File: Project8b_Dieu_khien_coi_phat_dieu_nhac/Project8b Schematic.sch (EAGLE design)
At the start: 16 parts, among them U1 ARDUINOR3-BPLACE

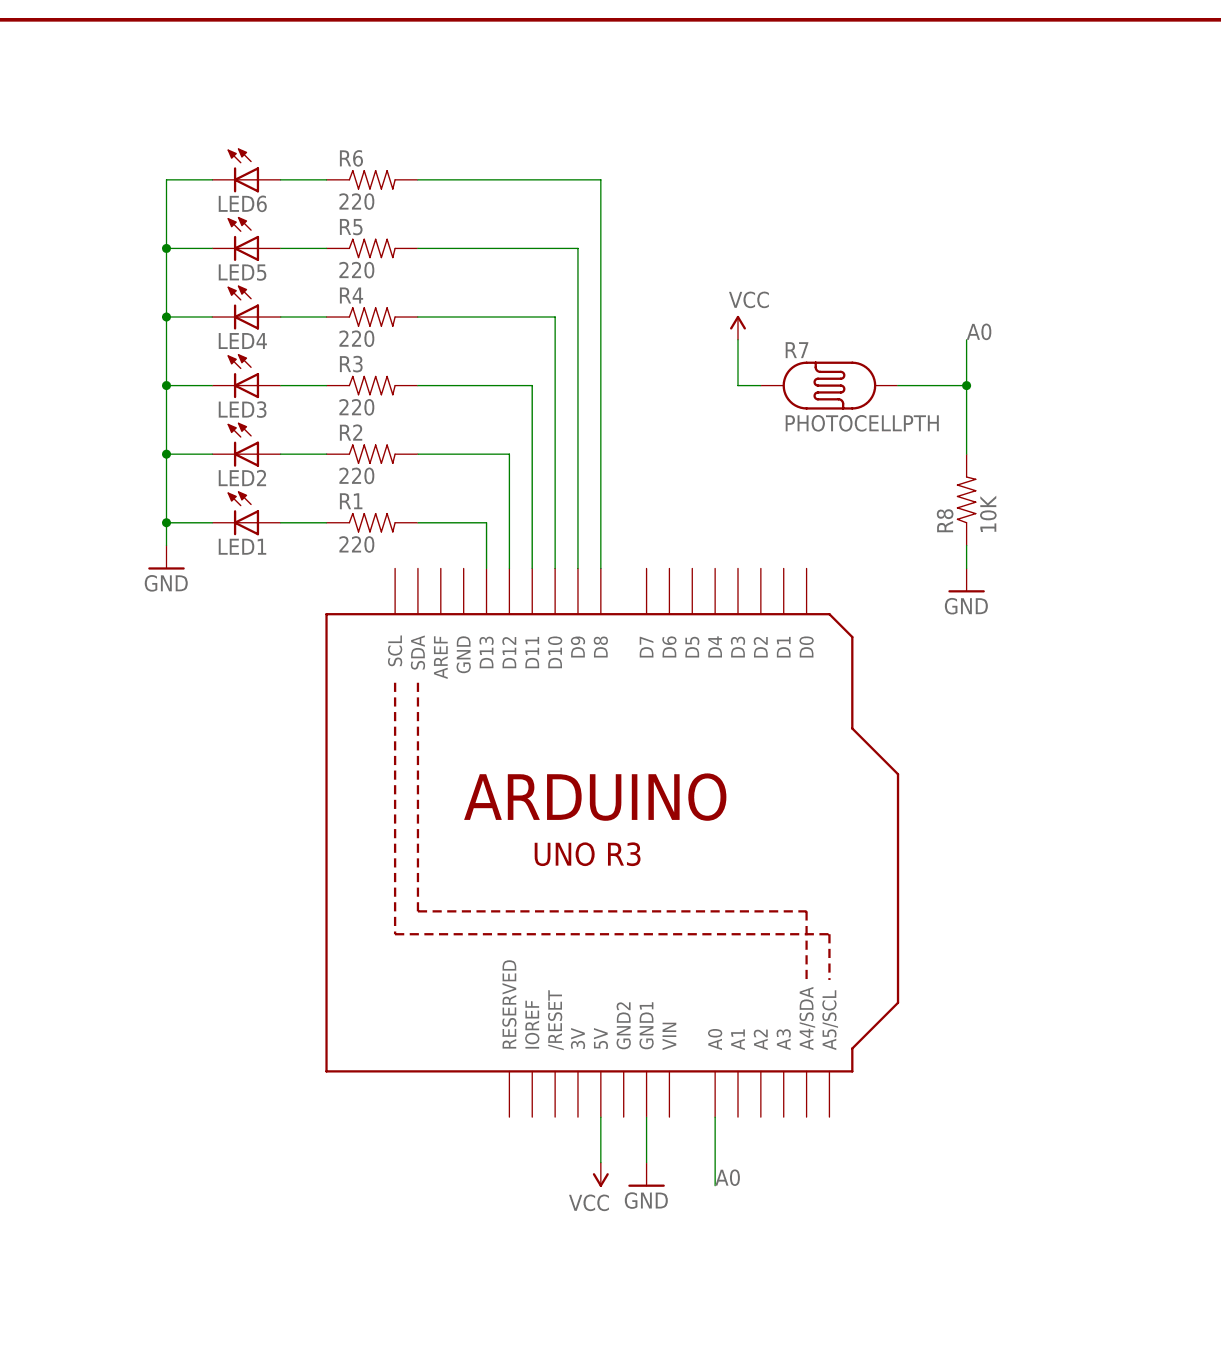
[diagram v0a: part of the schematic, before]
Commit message: Update schematic, breadboard cho nhieu projects.
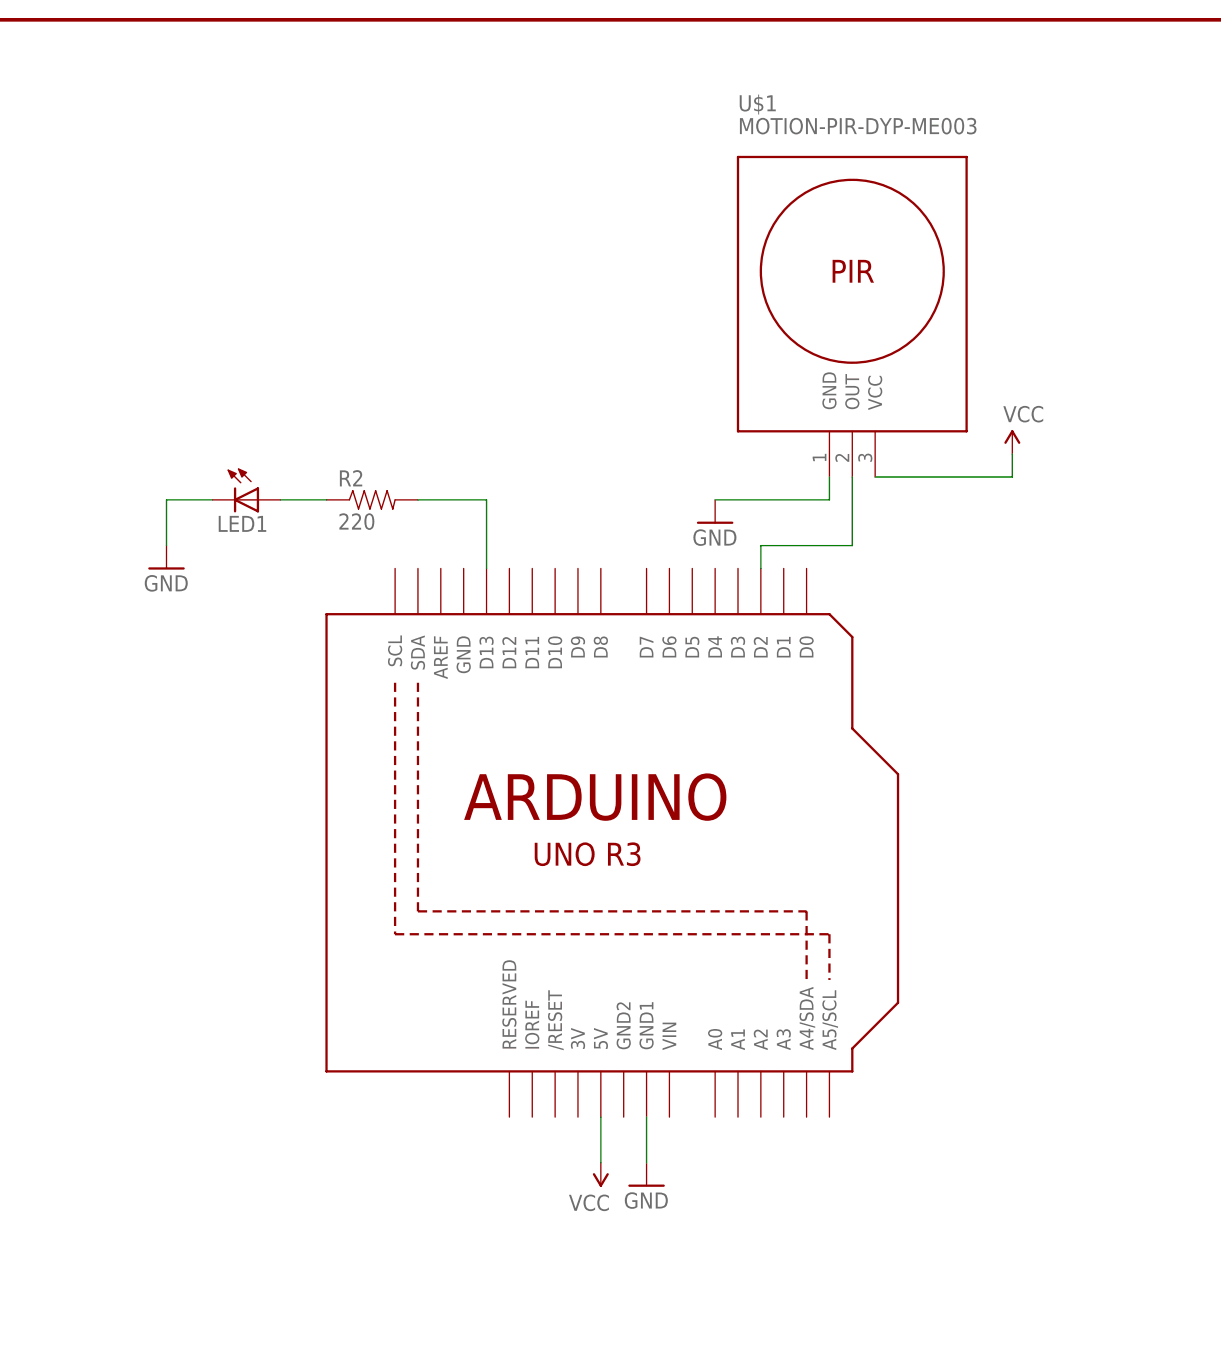
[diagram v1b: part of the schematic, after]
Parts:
- removed LED2, LED3, LED4, LED5, LED6: (no value), adafruit:LED
- removed R1, R3, R4, R5, R6: 220, SparkFun-Passives:RESISTOR0402-RES
- removed R7: PHOTOCELLPTH, SparkFun-Sensors:PHOTOCELLPTH
- removed R8: 10K, SparkFun-Passives:RESISTOR0402-RES
- added U$1: MOTION-PIR-DYP-ME003, diy-modules:MOTION-PIR-DYP-ME003
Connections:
- removed net A0: R7.P$2, R8.2, U1.A0
- removed net N$10: LED5.A, R5.1
- removed net N$11: LED4.A, R4.1
- removed net N$12: R6.2, U1.D8
- removed net N$13: R5.2, U1.D9
- removed net N$14: R4.2, U1.D10
- removed net N$4: LED3.A, R3.1
- removed net N$5: LED2.A, R2.1
- removed net N$6: R3.2, U1.D11
- removed net N$7: R2.2, U1.D12
- removed net N$9: LED6.A, R6.1
- new net N$3: U$1.OUT, U1.D2
- net GND: now also U$1.GND; no longer LED2.C, LED3.C, LED4.C, LED5.C, LED6.C, R8.1
- net N$1: now also R2.2; no longer R1.2
- net N$2: now also R2.1; no longer R1.1
- net VCC: now also U$1.VCC; no longer R7.P$1
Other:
- moved on the sheet: LED1, R2

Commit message: Thay doi schematic cua projects.
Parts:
- removed LED1: (no value), adafruit:LED
- removed R2: 220, SparkFun-Passives:RESISTOR0402-RES
- added SG1: BUZZERPTH-KIT, SparkFun-Electromechanical:BUZZERPTH-KIT
- renumbered U$1 to U2
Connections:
- removed net N$2: LED1.A, R2.1
- net GND: now also SG1.1; no longer LED1.C
- net N$1: now also SG1.2, U1.D9; no longer R2.2, U1.D13
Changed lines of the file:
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@@
 <?xml version="1.0" encoding="utf-8"?>
 <!DOCTYPE eagle SYSTEM "eagle.dtd">
-<eagle version="7.2.0">
+<eagle version="7.3.0">
 <drawing>
 <settings>
@@
 <layer number="223" name="223bmp" color="24" fill="1" visible="no" active="no"/>
 <layer number="224" name="224bmp" color="25" fill="1" visible="no" active="no"/>
+<layer number="225" name="225bmp" color="7" fill="1" visible="yes" active="yes"/>
+<layer number="226" name="226bmp" color="7" fill="1" visible="yes" active="yes"/>
+<layer number="227" name="227bmp" color="7" fill="1" visible="yes" active="yes"/>
+<layer number="228" name="228bmp" color="7" fill="1" visible="yes" active="yes"/>
+<layer number="229" name="229bmp" color="7" fill="1" visible="yes" active="yes"/>
+<layer number="230" name="230bmp" color="7" fill="1" visible="yes" active="yes"/>
 <layer number="231" name="Eagle3D_PG1" color="7" fill="1" visible="no" active="no"/>
 <layer number="232" name="Eagle3D_PG2" color="7" fill="1" visible="no" active="no"/>
@@
 <part name="SUPPLY1" library="SparkFun-Aesthetics" deviceset="VCC" device=""/>
 <part name="GND1" library="SparkFun-Aesthetics" deviceset="GND" device=""/>
-<part name="R2" library="SparkFun-Passives" deviceset="RESISTOR" device="0402-RES" value="220"/>
-<part name="LED1" library="adafruit" deviceset="LED" device=""/>
 <part name="GND2" library="SparkFun-Aesthetics" deviceset="GND" device=""/>
 <part name="GND3" library="SparkFun-Aesthetics" deviceset="GND" device=""/>
 <part name="SUPPLY2" library="SparkFun-Aesthetics" deviceset="VCC" device=""/>
 <part name="FRAME1" library="SparkFun-Aesthetics" deviceset="FRAME-LETTER" device=""/>
-<part name="U$1" library="diy-modules" deviceset="MOTION-PIR-DYP-ME003" device=""/>
+<part name="U2" library="diy-modules" deviceset="MOTION-PIR-DYP-ME003" device=""/>
+<part name="SG1" library="SparkFun-Electromechanical" deviceset="BUZZER" device="PTH-KIT"/>
 </parts>
 <sheets>
@@
 <instance part="SUPPLY1" gate="G$1" x="76.2" y="43.18" rot="R180"/>
 <instance part="GND1" gate="1" x="81.28" y="40.64"/>
-<instance part="R2" gate="G$1" x="50.8" y="116.84"/>
-<instance part="LED1" gate="G$1" x="38.1" y="116.84" rot="R270"/>
-<instance part="GND2" gate="1" x="27.94" y="109.22"/>
+<instance part="GND2" gate="1" x="50.8" y="114.3"/>
 <instance part="GND3" gate="1" x="88.9" y="114.3"/>
 <instance part="SUPPLY2" gate="G$1" x="121.92" y="121.92"/>
 <instance part="FRAME1" gate="G$1" x="-33.02" y="-15.24"/>
 <instance part="FRAME1" gate="V" x="114.3" y="-15.24"/>
-<instance part="U$1" gate="G$1" x="104.14" y="139.7"/>
+<instance part="U2" gate="G$1" x="104.14" y="139.7"/>
+<instance part="SG1" gate="G$1" x="63.5" y="121.92"/>
 </instances>
 <busses>
@@
 </segment>
 <segment>
-<pinref part="U$1" gate="G$1" pin="VCC"/>
+<pinref part="U2" gate="G$1" pin="VCC"/>
 <pinref part="SUPPLY2" gate="G$1" pin="VCC"/>
 <wire x1="106.68" y1="119.38" x2="121.92" y2="119.38" width="0.1524" layer="91"/>
@@
 </segment>
 <segment>
-<pinref part="GND2" gate="1" pin="GND"/>
-<pinref part="LED1" gate="G$1" pin="C"/>
-<wire x1="33.02" y1="116.84" x2="27.94" y2="116.84" width="0.1524" layer="91"/>
-<wire x1="27.94" y1="116.84" x2="27.94" y2="111.76" width="0.1524" layer="91"/>
-</segment>
-<segment>
 <pinref part="GND3" gate="1" pin="GND"/>
-<pinref part="U$1" gate="G$1" pin="GND"/>
+<pinref part="U2" gate="G$1" pin="GND"/>
 <wire x1="88.9" y1="116.84" x2="101.6" y2="116.84" width="0.1524" layer="91"/>
 <wire x1="101.6" y1="116.84" x2="101.6" y2="119.38" width="0.1524" layer="91"/>
 </segment>
-</net>
-<net name="N$1" class="0">
-<segment>
-<pinref part="R2" gate="G$1" pin="2"/>
-<pinref part="U1" gate="G$1" pin="D13"/>
-<wire x1="55.88" y1="116.84" x2="63.5" y2="116.84" width="0.1524" layer="91"/>
-<wire x1="63.5" y1="116.84" x2="63.5" y2="109.22" width="0.1524" layer="91"/>
-</segment>
-</net>
-<net name="N$2" class="0">
-<segment>
-<pinref part="R2" gate="G$1" pin="1"/>
-<pinref part="LED1" gate="G$1" pin="A"/>
-<wire x1="45.72" y1="116.84" x2="40.64" y2="116.84" width="0.1524" layer="91"/>
+<segment>
+<pinref part="SG1" gate="G$1" pin="1"/>
+<wire x1="63.5" y1="119.38" x2="50.8" y2="119.38" width="0.1524" layer="91"/>
+<pinref part="GND2" gate="1" pin="GND"/>
+<wire x1="50.8" y1="119.38" x2="50.8" y2="116.84" width="0.1524" layer="91"/>
 </segment>
 </net>
 <net name="N$3" class="0">
 <segment>
-<pinref part="U$1" gate="G$1" pin="OUT"/>
+<pinref part="U2" gate="G$1" pin="OUT"/>
 <wire x1="104.14" y1="119.38" x2="104.14" y2="111.76" width="0.1524" layer="91"/>
 <wire x1="104.14" y1="111.76" x2="93.98" y2="111.76" width="0.1524" layer="91"/>
@@
 </segment>
 </net>
+<net name="N$1" class="0">
+<segment>
+<pinref part="U1" gate="G$1" pin="D9"/>
+<wire x1="73.66" y1="109.22" x2="73.66" y2="119.38" width="0.1524" layer="91"/>
+<pinref part="SG1" gate="G$1" pin="2"/>
+<wire x1="73.66" y1="119.38" x2="66.04" y2="119.38" width="0.1524" layer="91"/>
+</segment>
+</net>
